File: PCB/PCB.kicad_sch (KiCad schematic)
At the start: 9 parts, among them J1 Servo_Conn_1, J2 Servo_Conn_2, J3 Servo_Conn_3, J4 Servo_Conn_4, J5 Servo_Conn_5, J6 Servo_Conn_6

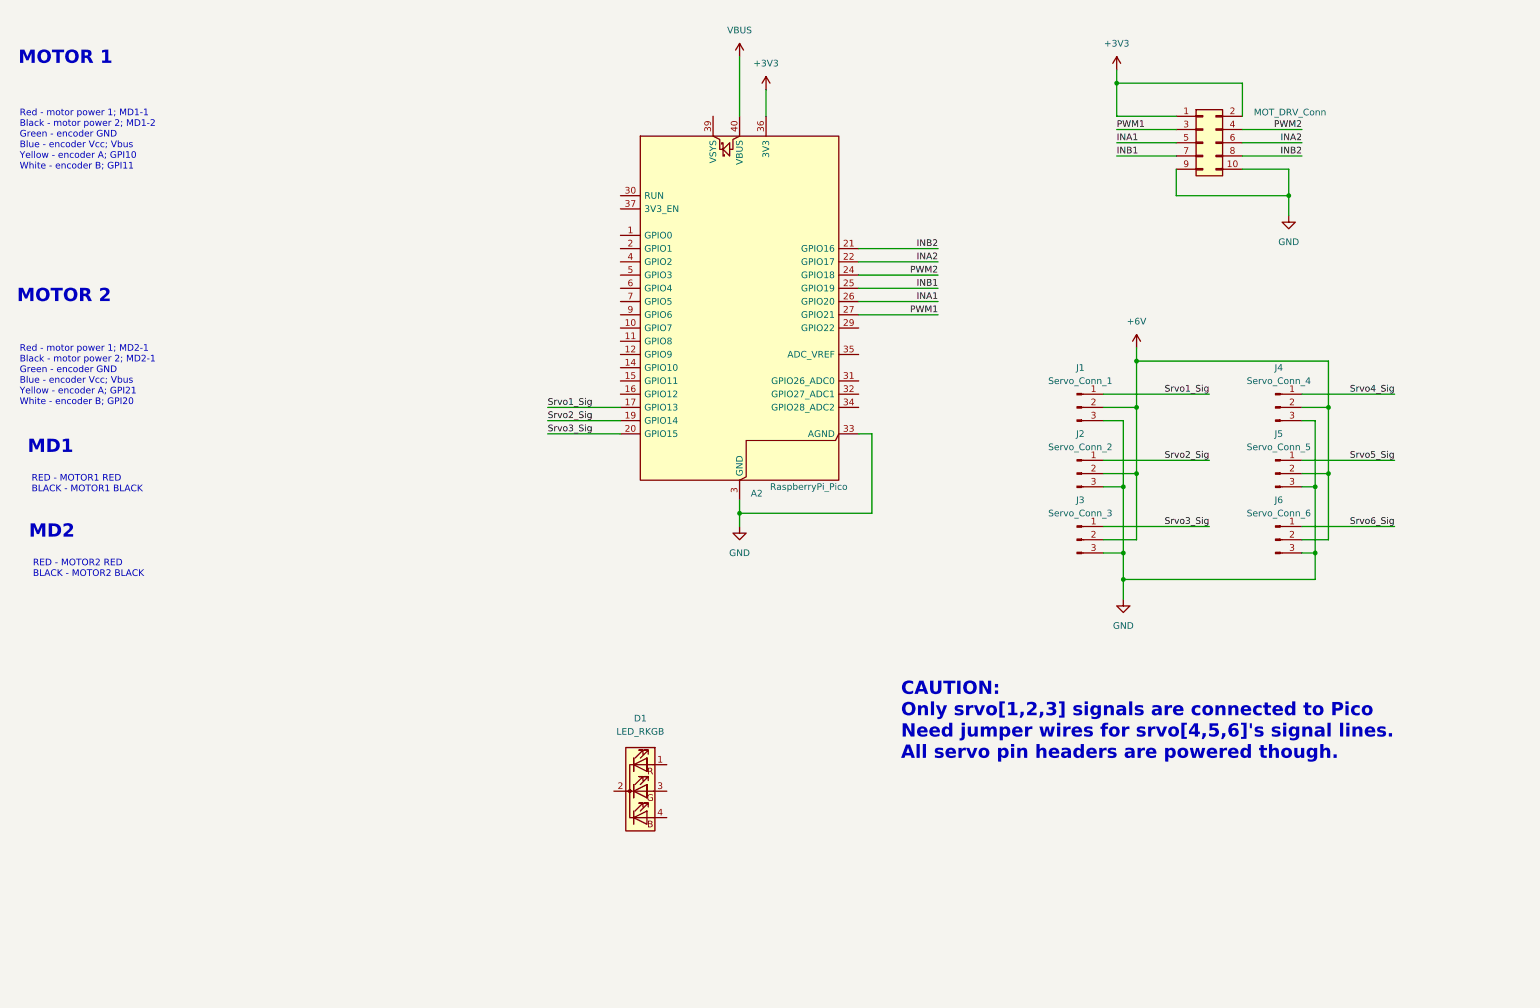
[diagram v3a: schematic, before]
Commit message: update motor connections
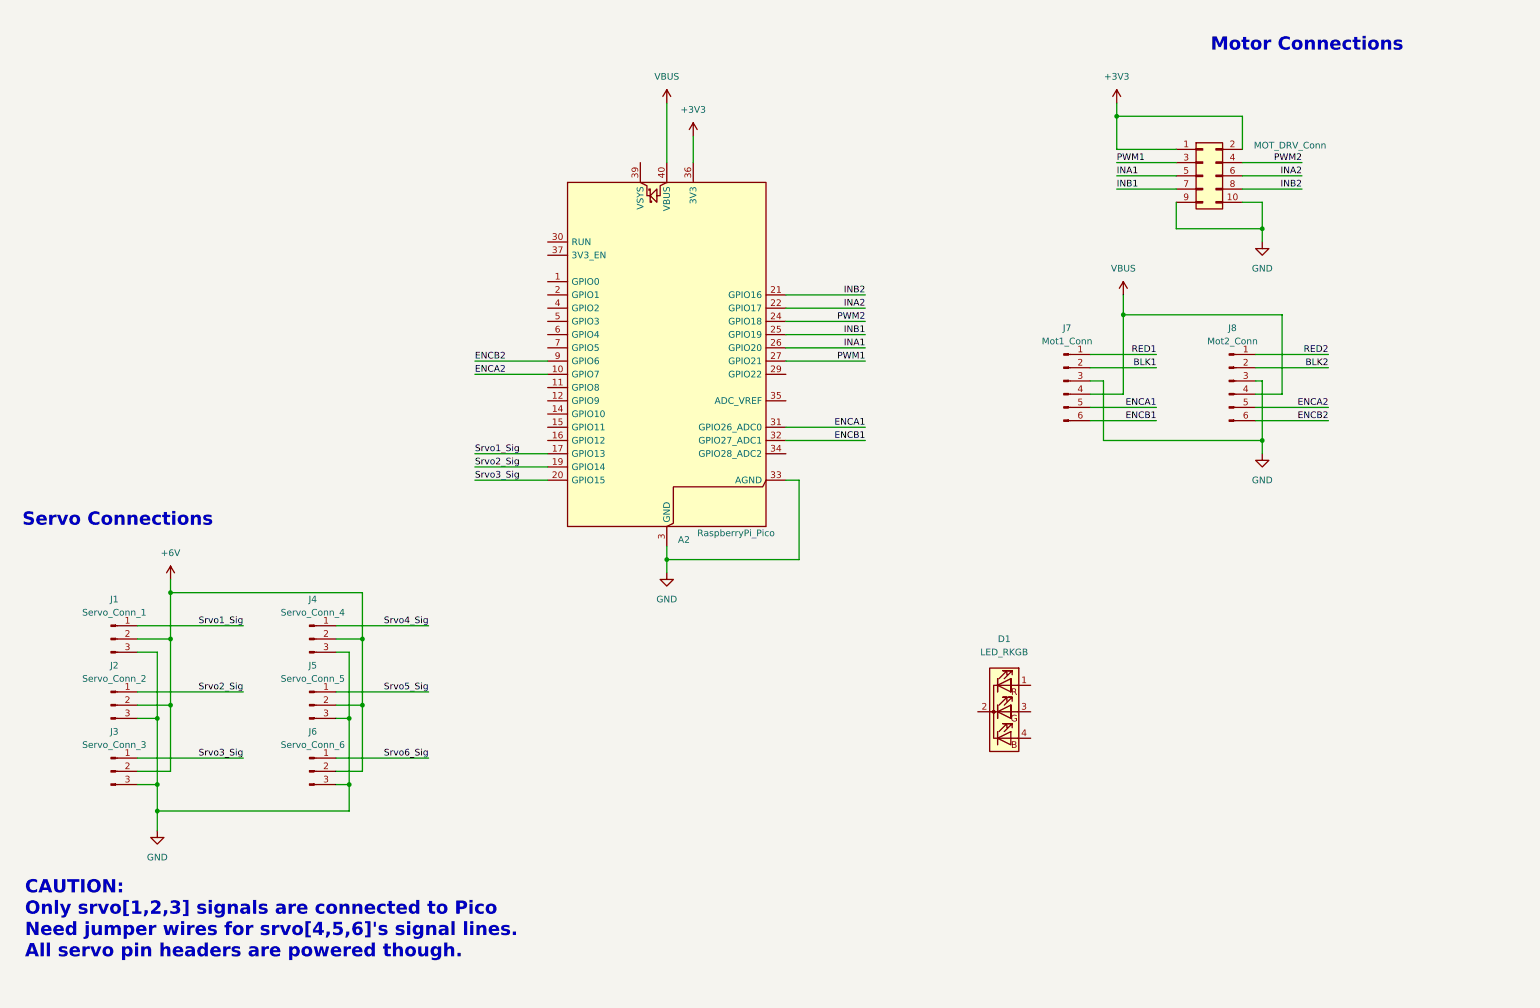
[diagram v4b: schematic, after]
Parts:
- added J7: Mot1_Conn, symbol Connector:Conn_01x06_Pin
- added J8: Mot2_Conn, symbol Connector:Conn_01x06_Pin
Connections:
- net GND: now also J7.3 (Pin_3), J8.3 (Pin_3)
- net VBUS: now also J7.4 (Pin_4), J8.4 (Pin_4)
- net ENCA2: now reaches A2.10 (GPIO7)
- net ENCA2: now also J8.5 (Pin_5)
- net ENCA1: now reaches A2.31 (GPIO26_ADC0)
- net ENCA1: now also J7.5 (Pin_5)
- net ENCB1: now reaches A2.32 (GPIO27_ADC1)
- net ENCB1: now also J7.6 (Pin_6)
- net ENCB2: now reaches A2.9 (GPIO6)
- net ENCB2: now also J8.6 (Pin_6)
- new net BLK1: J7.2 (Pin_2)
- new net BLK2: J8.2 (Pin_2)
- new net RED1: J7.1 (Pin_1)
- new net RED2: J8.1 (Pin_1)
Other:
- note added: "Motor Connections"
- note added: "Servo Connections"
- note removed: "MD1"
- note removed: "MD2"
- note removed: "MOTOR 1"
- note removed: "MOTOR 2"
- note removed: "RED - MOTOR1 RED BLACK - MOTOR1 BLACK"
- note removed: "RED - MOTOR2 RED BLACK - MOTOR2 BLACK"
- note removed: "Red - motor power 1; MD1-1 Black - motor power 2; MD1-2 Green - encoder GND Blue - encoder Vcc; Vbus Yellow - encoder A; GPI10 White - encoder B; GPI11"
- note removed: "Red - motor power 1; MD2-1 Black - motor power 2; MD2-1 Green - encoder GND Blue - encoder Vcc; Vbus Yellow - encoder A; GPI21 White - encoder B; GPI20"
- moved on the sheet: A2, D1, J1, J2, J3, J4, J5, J6, MOT_DRV_Conn

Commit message: update peripheral connections
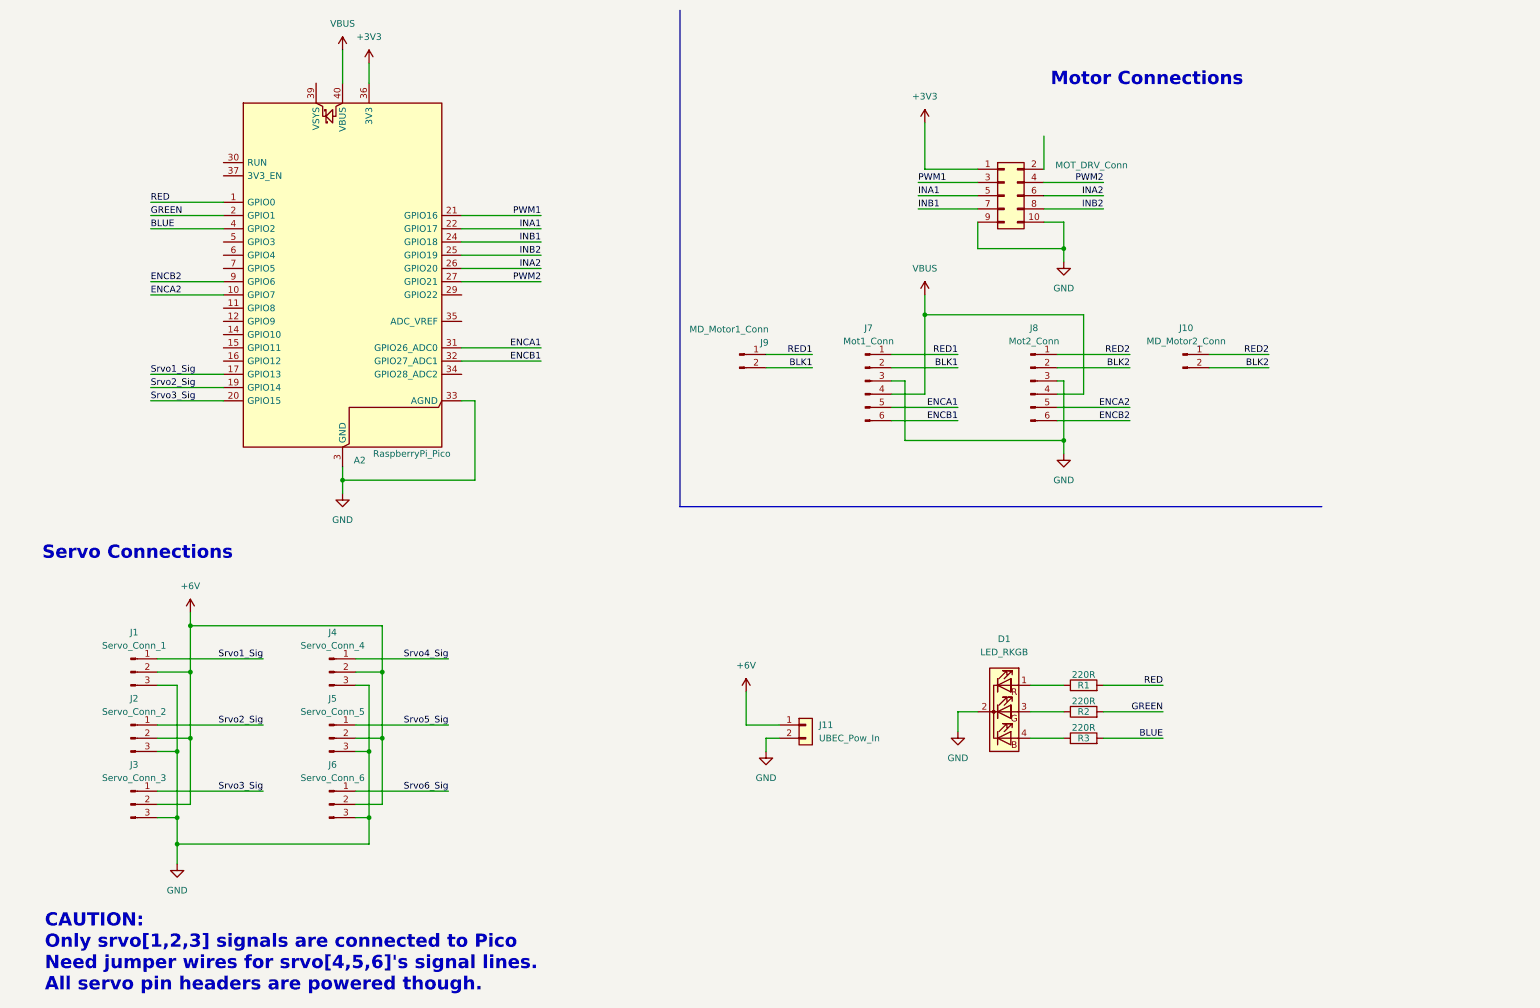
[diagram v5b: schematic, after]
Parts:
- added J10: MD_Motor2_Conn, symbol Connector:Conn_01x02_Pin
- added J11: UBEC_Pow_In, symbol Connector_Generic:Conn_01x02
- added J9: MD_Motor1_Conn, symbol Connector:Conn_01x02_Pin
- added R1, R2, R3: 220R, symbol Device:R
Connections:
- net +3V3: no longer MOT_DRV_Conn.2 (Pin_2)
- net +6V: now also J11.1 (Pin_1)
- net BLK1: now also J9.2 (Pin_2)
- net BLK2: now also J10.2 (Pin_2)
- net GND: now also D1.2 (K), J11.2 (Pin_2)
- net INA1: now also A2.22 (GPIO17); no longer A2.26 (GPIO20)
- net INA2: now also A2.26 (GPIO20); no longer A2.22 (GPIO17)
- net INB1: now also A2.24 (GPIO18); no longer A2.25 (GPIO19)
- net INB2: now also A2.25 (GPIO19); no longer A2.21 (GPIO16)
- net PWM1: now also A2.21 (GPIO16); no longer A2.27 (GPIO21)
- net PWM2: now also A2.27 (GPIO21); no longer A2.24 (GPIO18)
- net RED1: now also J9.1 (Pin_1)
- net RED2: now also J10.1 (Pin_1)
- net at D1.1 (RA): now also R1.1
- net at D1.3 (GA): now also R2.1
- net at D1.4 (BA): now also R3.1
- net RED: now reaches A2.1 (GPIO0)
- net RED: now also R1.2
- net GREEN: now reaches A2.2 (GPIO1)
- net GREEN: now also R2.2
- net BLUE: now reaches A2.4 (GPIO2)
- net BLUE: now also R3.2
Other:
- moved on the sheet: A2, J1, J2, J3, J4, J5, J6, J7, J8, MOT_DRV_Conn

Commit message: update sch
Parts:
- removed J10: MD_Motor2_Conn, symbol Connector:Conn_01x02_Pin
- removed J9: MD_Motor1_Conn, symbol Connector:Conn_01x02_Pin
- added J10, J9: Conn_01x04_Pin, symbol Connector:Conn_01x04_Pin
- added J12: Spare_GPIO_Conn, symbol Connector:Conn_01x10_Pin
- renumbered MOT_DRV_Conn to MOT_DRV_Conn1
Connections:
- net +3V3: now also MOT_DRV_Conn1.2 (Pin_2)
- net BLK1: now also J9.3 (Pin_3), J9.4 (Pin_4)
- net BLK2: now also J10.3 (Pin_3), J10.4 (Pin_4)
- net GND: now also J12.4 (Pin_4), J12.7 (Pin_7)
- net RED1: now also J9.1 (Pin_1), J9.2 (Pin_2)
- net RED2: now also J10.1 (Pin_1), J10.2 (Pin_2)
- net Srvo1_Sig: now also A2.20 (GPIO15); no longer A2.17 (GPIO13)
- net Srvo3_Sig: now also A2.17 (GPIO13); no longer A2.20 (GPIO15)
- net GPIO8: now reaches A2.11 (GPIO8)
- net GPIO8: now also J12.5 (Pin_5)
- net GPIO9: now reaches A2.12 (GPIO9)
- net GPIO9: now also J12.6 (Pin_6)
- net GPIO10: now reaches A2.14 (GPIO10)
- net GPIO10: now also J12.8 (Pin_8)
- net GPIO11: now reaches A2.15 (GPIO11)
- net GPIO11: now also J12.9 (Pin_9)
- net GPIO12: now reaches A2.16 (GPIO12)
- net GPIO12: now also J12.10 (Pin_10)
- net GPIO22: now reaches A2.29 (GPIO22)
- net GPIO28: now reaches A2.34 (GPIO28_ADC2)
- net 5VIN: now reaches A2.39 (VSYS)
- net GPIO3: now reaches A2.5 (GPIO3)
- net GPIO3: now also J12.1 (Pin_1)
- net GPIO4: now reaches A2.6 (GPIO4)
- net GPIO4: now also J12.2 (Pin_2)
- net GPIO5: now reaches A2.7 (GPIO5)
- net GPIO5: now also J12.3 (Pin_3)
- no-connect marks 0 -> 3
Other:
- moved on the sheet: D1, J11, R1, R2, R3

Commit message: assign footprints
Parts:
- D1: footprint (none) -> LED_THT:LED_D5.0mm-4_RGB_Wide_Pins
- J1, J2, J3, J4, J5, J6: footprint (none) -> Connector_PinHeader_2.54mm:PinHeader_1x03_P2.54mm_Vertical
- J10, J9: footprint (none) -> Connector_PinHeader_2.54mm:PinHeader_1x04_P2.54mm_Vertical
- J11: footprint (none) -> Connector_PinHeader_2.54mm:PinHeader_1x02_P2.54mm_Horizontal
- J12: footprint (none) -> Connector_PinHeader_2.54mm:PinHeader_1x10_P2.54mm_Vertical
- J7, J8: footprint (none) -> Connector_PinHeader_2.54mm:PinHeader_1x06_P2.54mm_Vertical
- R1, R2, R3: footprint (none) -> Resistor_THT:R_Axial_DIN0207_L6.3mm_D2.5mm_P7.62mm_Horizontal
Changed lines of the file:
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@@
 			)
 		)
-		(property "Footprint" ""
+		(property "Footprint" "Connector_PinHeader_2.54mm:PinHeader_1x06_P2.54mm_Vertical"
 			(at 210.82 83.82 0)
 			(effects
@@
 			)
 		)
-		(property "Footprint" ""
+		(property "Footprint" "Connector_PinHeader_2.54mm:PinHeader_1x03_P2.54mm_Vertical"
 			(at 38.1 139.7 0)
 			(effects
@@
 			)
 		)
-		(property "Footprint" ""
+		(property "Footprint" "Connector_PinHeader_2.54mm:PinHeader_1x02_P2.54mm_Horizontal"
 			(at 161.29 135.89 0)
 			(effects
@@
 			)
 		)
-		(property "Footprint" ""
+		(property "Footprint" "Connector_PinHeader_2.54mm:PinHeader_1x03_P2.54mm_Vertical"
 			(at 76.2 165.1 0)
 			(effects
@@
 			)
 		)
-		(property "Footprint" ""
+		(property "Footprint" "LED_THT:LED_D5.0mm-4_RGB_Wide_Pins"
 			(at 189.23 139.7 0)
 			(effects
@@
 			)
 		)
-		(property "Footprint" ""
+		(property "Footprint" "Resistor_THT:R_Axial_DIN0207_L6.3mm_D2.5mm_P7.62mm_Horizontal"
 			(at 204.47 135.128 90)
 			(effects
@@
 			)
 		)
-		(property "Footprint" ""
+		(property "Footprint" "Connector_PinHeader_2.54mm:PinHeader_1x04_P2.54mm_Vertical"
 			(at 240.03 81.28 0)
 			(effects
@@
 			)
 		)
-		(property "Footprint" ""
+		(property "Footprint" "Connector_PinHeader_2.54mm:PinHeader_1x03_P2.54mm_Vertical"
 			(at 76.2 139.7 0)
 			(effects
@@
 			)
 		)
-		(property "Footprint" ""
+		(property "Footprint" "Connector_PinHeader_2.54mm:PinHeader_1x03_P2.54mm_Vertical"
 			(at 76.2 152.4 0)
 			(effects
@@
 			)
 		)
-		(property "Footprint" ""
+		(property "Footprint" "Resistor_THT:R_Axial_DIN0207_L6.3mm_D2.5mm_P7.62mm_Horizontal"
 			(at 204.47 140.208 90)
 			(effects
@@
 			)
 		)
-		(property "Footprint" ""
+		(property "Footprint" "Connector_PinHeader_2.54mm:PinHeader_1x03_P2.54mm_Vertical"
 			(at 38.1 152.4 0)
 			(effects
@@
 			)
 		)
-		(property "Footprint" ""
+		(property "Footprint" "Resistor_THT:R_Axial_DIN0207_L6.3mm_D2.5mm_P7.62mm_Horizontal"
 			(at 204.47 145.288 90)
 			(effects
@@
 			)
 		)
-		(property "Footprint" ""
+		(property "Footprint" "Connector_PinHeader_2.54mm:PinHeader_1x06_P2.54mm_Vertical"
 			(at 179.07 83.82 0)
 			(effects
@@
 			)
 		)
-		(property "Footprint" ""
+		(property "Footprint" "Connector_PinHeader_2.54mm:PinHeader_1x04_P2.54mm_Vertical"
 			(at 153.67 81.28 0)
 			(effects
@@
 			)
 		)
-		(property "Footprint" ""
+		(property "Footprint" "Connector_PinHeader_2.54mm:PinHeader_1x03_P2.54mm_Vertical"
 			(at 38.1 165.1 0)
 			(effects
@@
 			)
 		)
-		(property "Footprint" ""
+		(property "Footprint" "Connector_PinHeader_2.54mm:PinHeader_1x10_P2.54mm_Vertical"
 			(at 237.49 142.24 0)
 			(effects

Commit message: set mounting holes
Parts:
- added H1, H2, H3, H4: MountingHole_Pad, MountingHole:MountingHole_2.7mm_M2.5, symbol Mechanical:MountingHole_Pad
- A2: footprint Module:RaspberryPi_Pico_Common_Unspecified -> RaspberryPi_Pico_THT:RaspberryPi_Pico_THT
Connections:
- no-connect marks 3 -> 7
